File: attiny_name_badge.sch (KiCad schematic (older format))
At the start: 1 part, among them U1 ATtiny841-SSU

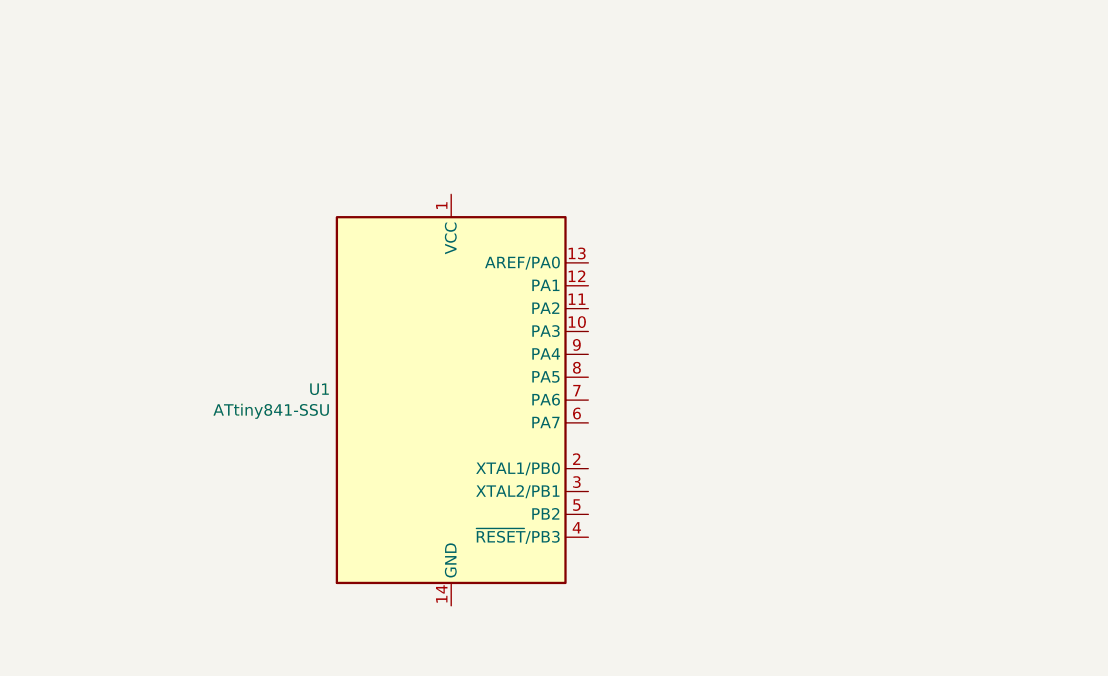
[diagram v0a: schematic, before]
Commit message: initial layout
custom 2032 cell holder
misc initial placements
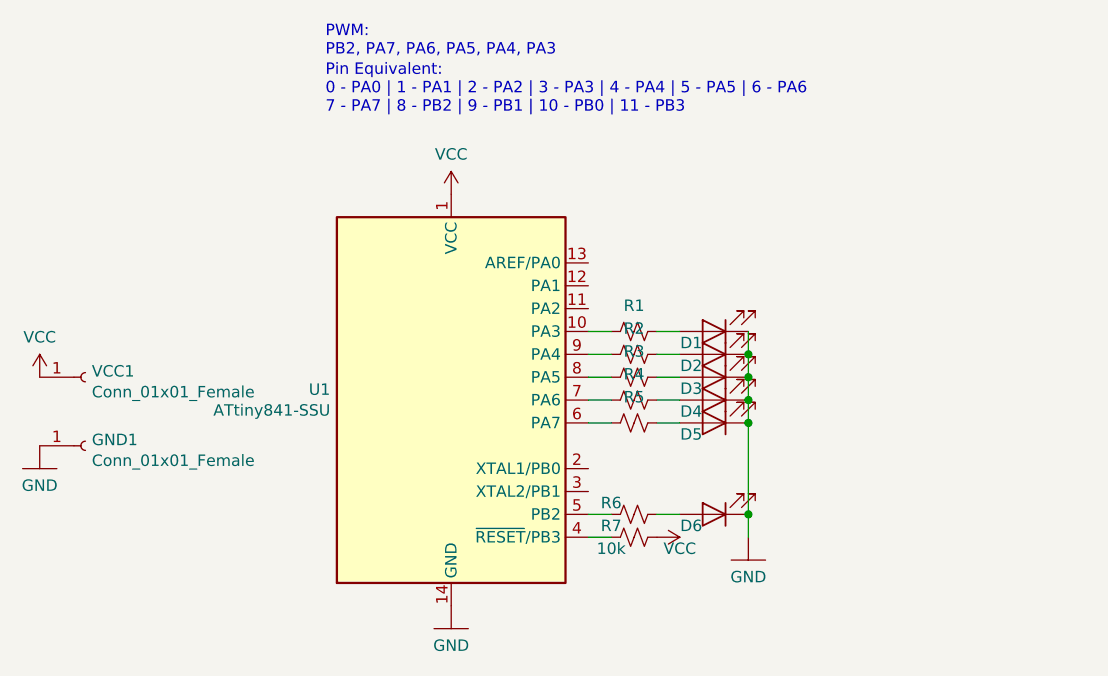
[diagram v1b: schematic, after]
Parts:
- added D1, D2, D3, D4, D5, D6: LED, LED_SMD:LED_0805_2012Metric_Pad1.15x1.40mm_HandSolder, symbol Device:LED
- added GND1, VCC1: Conn_01x01_Female, Connector_Pin:Pin_D1.0mm_L10.0mm_LooseFit, symbol Connector:Conn_01x01_Female
- added R1, R2, R3, R4, R5, R6: R_Small_US, LED_SMD:LED_0805_2012Metric_Pad1.15x1.40mm_HandSolder, symbol Device:R_Small_US
- added R7: 10k, LED_SMD:LED_0805_2012Metric_Pad1.15x1.40mm_HandSolder, symbol Device:R_Small_US
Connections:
- net VCC: now reaches U1.1 (VCC)
- net VCC: now also R7.1, VCC1.1 (Pin_1)
- net at U1.10 (PA3): now also R1.2
- net GND: now reaches U1.14 (GND)
- net GND: now also D1.1 (K), D2.1 (K), D3.1 (K), D4.1 (K), D5.1 (K), D6.1 (K), GND1.1 (Pin_1)
- net at U1.4 (~RESET~/PB3): now also R7.2
- net at U1.5 (PB2): now also R6.2
- net at U1.6 (PA7): now also R5.2
- net at U1.7 (PA6): now also R4.2
- net at U1.8 (PA5): now also R3.2
- net at U1.9 (PA4): now also R2.2
- new net: D1.2 (A), R1.1
- new net: D2.2 (A), R2.1
- new net: D3.2 (A), R3.1
- new net: D4.2 (A), R4.1
- new net: D5.2 (A), R5.1
- new net: D6.2 (A), R6.1
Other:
- note added: "PWM:\nPB2, PA7, PA6, PA5, PA4, PA3"
- note added: "Pin Equivalent:\n0 - PA0 | 1 - PA1 | 2 - PA2 | 3 - PA3 | 4 - PA4 | 5 - PA5 | 6 - PA6\n7 - PA7 | 8 - PB2 | 9 - PB1 | 10 - PB0 | 11 - PB3\n"

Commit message: working circuit
need name/finishing touches
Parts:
- added C1: CAP0805, Capacitor_SMD:C_0805_2012Metric_Pad1.15x1.40mm_HandSolder, symbol SparkFun-Capacitors:CAP0805
- added D10, D11, D12, D7, D8, D9: LED, LED_SMD:LED_0805_2012Metric_Pad1.15x1.40mm_HandSolder, symbol Device:LED
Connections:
- net GND: now also C1.1, D10.1 (K), D11.1 (K), D12.1 (K), D7.1 (K), D8.1 (K), D9.1 (K)
- net VCC: now also C1.2
- net at D1.2 (A), R1.1: now also D7.2 (A)
- net at D2.2 (A), R2.1: now also D8.2 (A)
- net at D3.2 (A), R3.1: now also D9.2 (A)
- net at D4.2 (A), R4.1: now also D10.2 (A)
- net at D5.2 (A), R5.1: now also D11.2 (A)
- net at D6.2 (A), R6.1: now also D12.2 (A)
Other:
- moved on the sheet: D1, D2, D3, D4, D5, D6

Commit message: working board
cut 'er out!
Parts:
- added SW1: SW_DPST_x2, Button_Switch_THT:SW_PUSH_6mm_H5mm, symbol Switch:SW_DPST_x2
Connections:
- net VCC: now also SW1.2 (B); no longer U1.1 (VCC)
- new net: SW1.1 (A), U1.1 (VCC)
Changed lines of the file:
@@
 L SparkFun-Aesthetics:VCC #SUPPLY0101
 U 1 1 5D696DEA
-P 6100 2300
-F 0 "#SUPPLY0101" H 6100 2300 50  0001 L BNN
-F 1 "VCC" V 6100 2429 50  0000 L CNN
-F 2 "" H 6100 2300 50  0001 C CNN
-F 3 "" H 6100 2300 50  0001 C CNN
-	1    6100 2300
+P 6500 2300
+F 0 "#SUPPLY0101" H 6500 2300 50  0001 L BNN
+F 1 "VCC" V 6500 2450 50  0000 L CNN
+F 2 "" H 6500 2300 50  0001 C CNN
+F 3 "" H 6500 2300 50  0001 C CNN
+	1    6500 2300
 	0    1    1    0
 $EndComp
@@
 	7400 3850 7400 3750
 Connection ~ 7400 3750
-Wire Wire Line
-	7400 3750 7400 3850
 Connection ~ 4300 3500
 Connection ~ 4300 3200
+$Comp
+L Switch:SW_DPST_x2 SW1
+U 1 1 5D7BF4E8
+P 6300 2300
+F 0 "SW1" H 6300 2535 50  0000 C CNN
+F 1 "SW_DPST_x2" H 6300 2444 50  0000 C CNN
+F 2 "Button_Switch_THT:SW_PUSH_6mm_H5mm" H 6300 2300 50  0001 C CNN
+F 3 "~" H 6300 2300 50  0001 C CNN
+	1    6300 2300
+	1    0    0    -1
+$EndComp
 $EndSCHEMATC
